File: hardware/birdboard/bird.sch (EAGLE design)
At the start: 39 parts, among them IC1 ATMEGA88-THIN

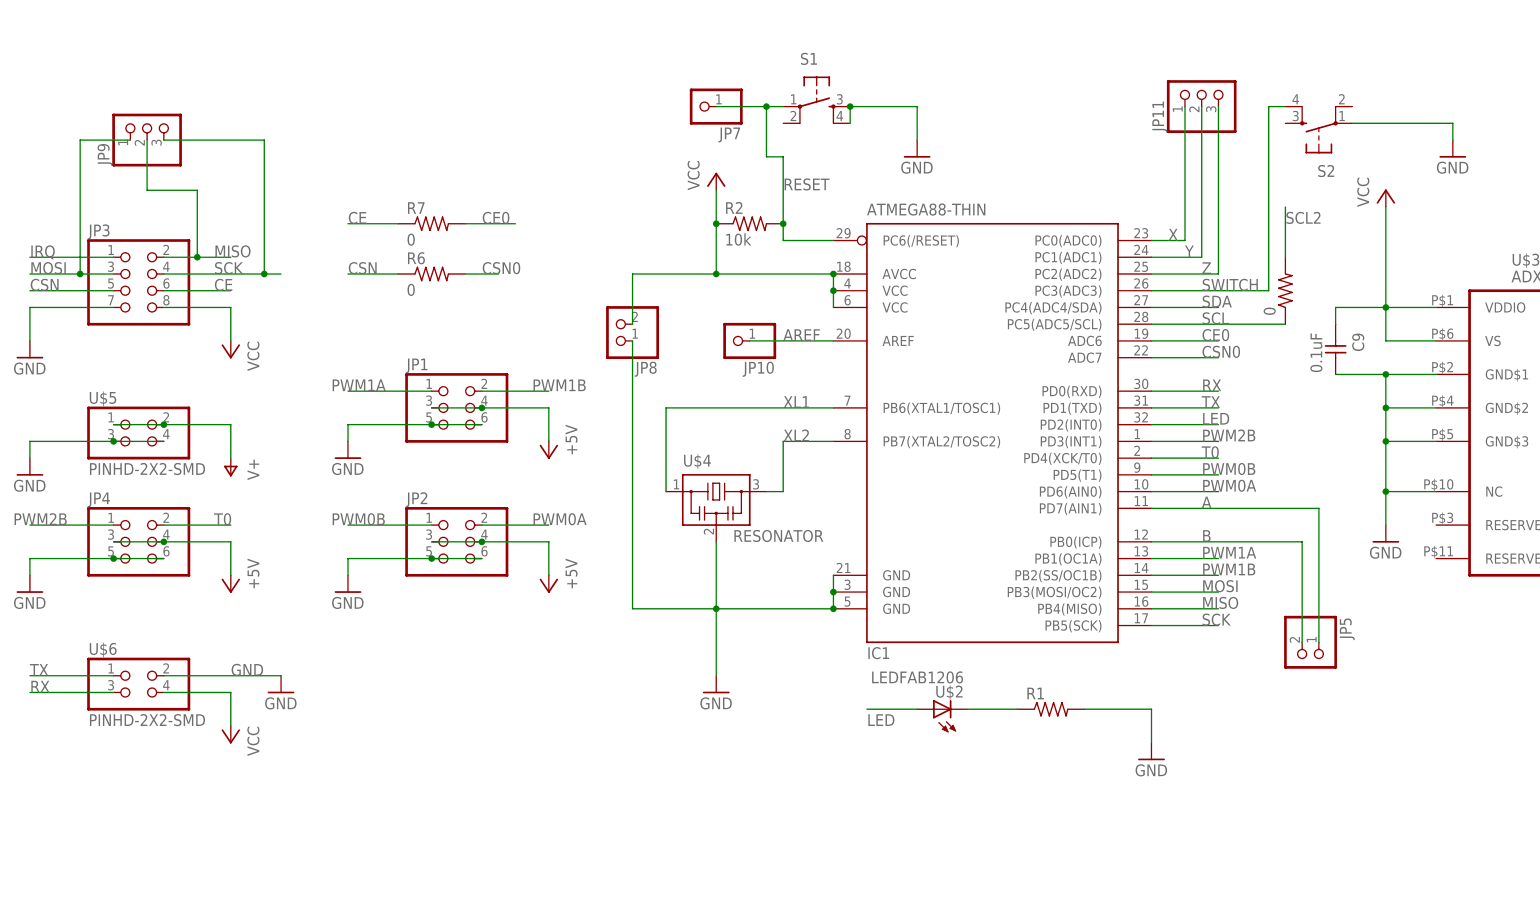
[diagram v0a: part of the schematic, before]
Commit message: Remove DigialIO since we don't need software implementations, updated bird board to newer version
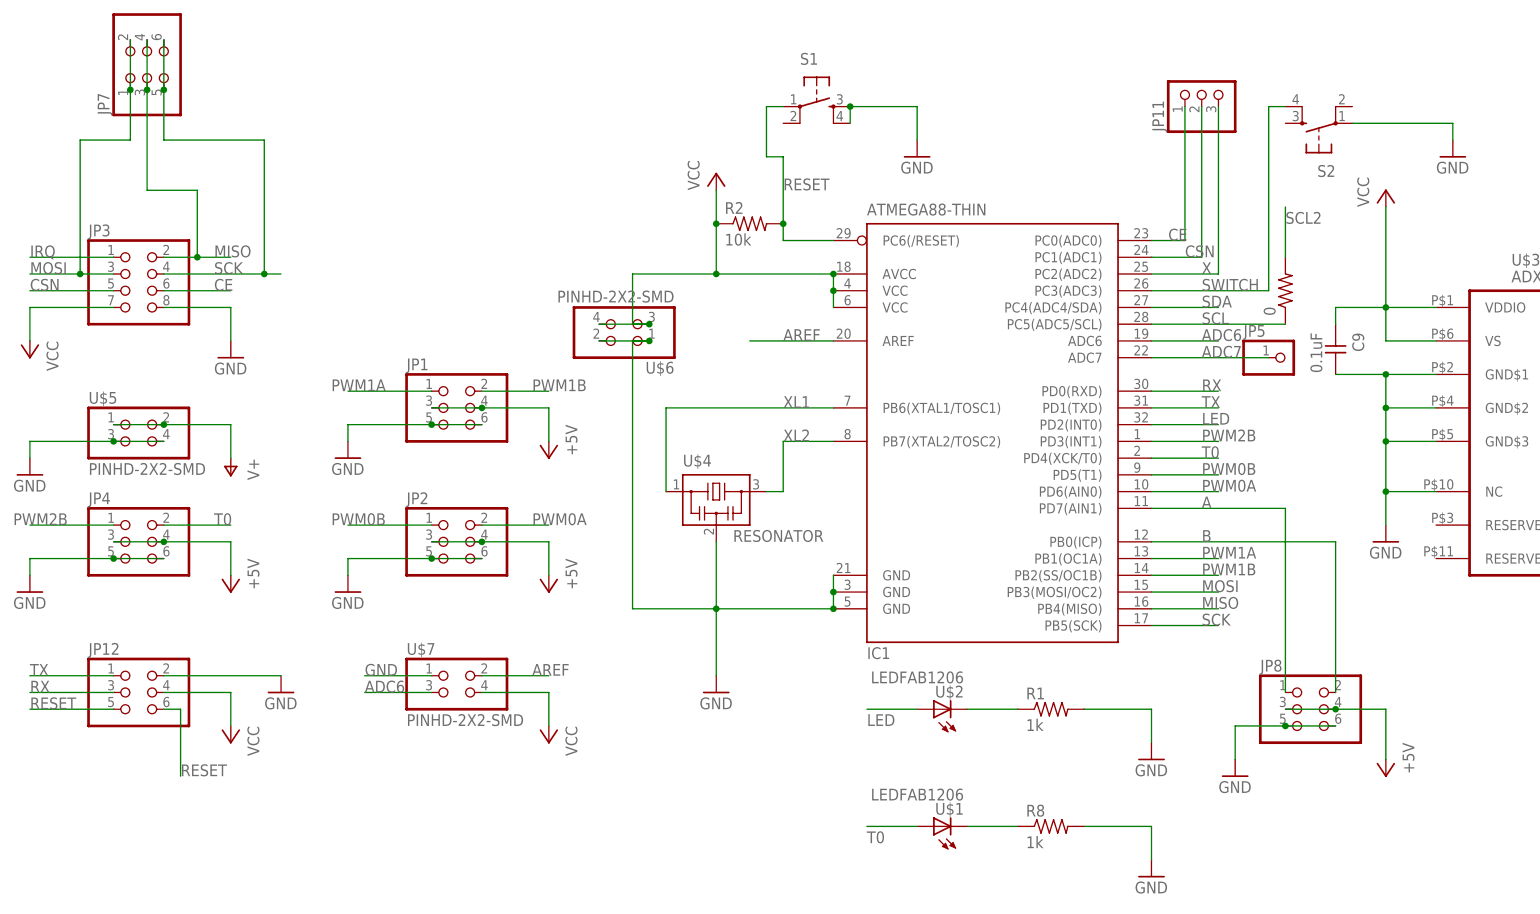
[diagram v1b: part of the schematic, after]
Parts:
- removed JP10: (no value), pinhead+:PINHD-1X1
- removed JP9: (no value), pinhead+:PINHD-1X3
- removed R6, R7: 0, fab:RES-US1206FAB
- added JP12: (no value), fab:PINHD-2X3-SMD
- added R8: 1k, fab:RES-US1206FAB
- added U$1: LEDFAB1206, fab:LEDFAB1206
- added U$7: PINHD-2X2-SMD, fab:PINHD-2X2-SMD
- JP5: device pinhead:PINHD-1X2 -> pinhead:PINHD-1X1
- JP7: device pinhead+:PINHD-1X1 -> fab:PINHD-2X3-SMD
- JP8: device pinhead:PINHD-1X2 -> fab:PINHD-2X3-SMD
- R1: value (none) -> 1k
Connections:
- removed net CE0: IC1.ADC6, R7.2
- removed net CSN0: IC1.ADC7, R6.2
- removed net Y: IC1.PC1(ADC1), JP11.2
- removed net Z: IC1.PC2(ADC2), JP11.3
- new net ADC6: IC1.ADC6, U$7.3
- new net ADC7: IC1.ADC7, JP5.1
- new net N$3: R8.1, U$1.C
- net +5V: now also JP8.3, JP8.4
- net A: now also JP8.1; no longer JP5.1
- net AREF: now also U$7.2; no longer JP10.1
- net B: now also JP8.2; no longer JP5.2
- net CE: now also IC1.PC0(ADC0), JP11.1; no longer R7.1
- net CSN: now also IC1.PC1(ADC1), JP11.2; no longer R6.1
- net GND: now also JP12.2, JP3.8, JP8.5, JP8.6, R8.2, U$6.1, U$7.1; no longer JP3.7, JP8.1
- net MISO: now also JP7.3, JP7.4; no longer JP9.2
- net MOSI: now also JP7.1, JP7.2; no longer JP9.1
- net RESET: now also JP12.5, JP12.6; no longer JP7.1
- net RX: now also JP12.3; no longer U$6.3
- net SCK: now also JP7.5, JP7.6; no longer JP9.3
- net T0: now also U$1.A
- net TX: now also JP12.1; no longer U$6.1
- net VCC: now also JP12.4, JP3.7, U$6.3, U$7.4; no longer JP3.8, JP8.2
- net X: now also IC1.PC2(ADC2), JP11.3; no longer IC1.PC0(ADC0), JP11.1
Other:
- moved on the sheet: U$6
